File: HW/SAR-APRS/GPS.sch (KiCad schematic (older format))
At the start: 12 parts

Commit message: schematic update
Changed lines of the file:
@@
 Wire Wire Line
 	8400 2425 8400 4675
-Text GLabel 3200 2425 0    50   Input ~ 0
+Text GLabel 3200 2425 0    50   Output ~ 0
 GPS_PPS
 Text GLabel 3200 3150 0    50   Input ~ 0
 GPS_RXD
-Text GLabel 3200 3050 0    50   Input ~ 0
+Text GLabel 3200 3050 0    50   Output ~ 0
 GPS_TXD
 Wire Wire Line

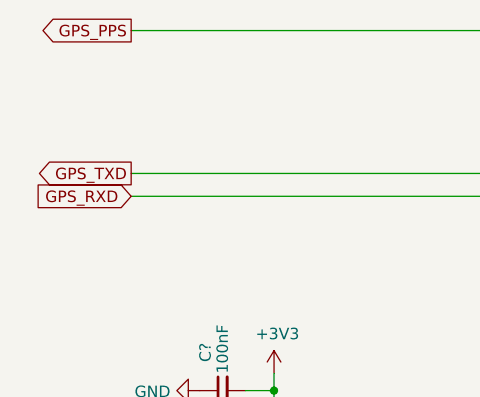
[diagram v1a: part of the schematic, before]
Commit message: schematic update
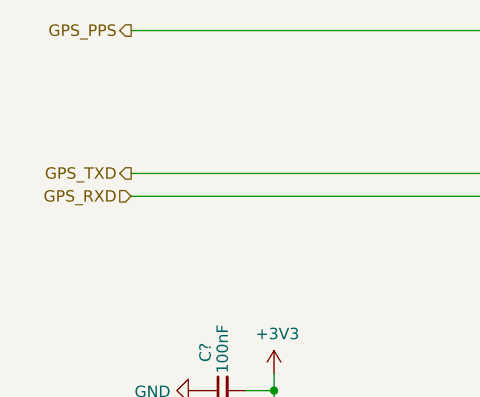
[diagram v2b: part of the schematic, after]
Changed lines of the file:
@@
 $Descr A4 11693 8268
 encoding utf-8
-Sheet 4 6
+Sheet 6 6
 Title ""
 Date ""
@@
 Wire Wire Line
 	8400 2425 8400 4675
-Text GLabel 3200 2425 0    50   Output ~ 0
+Wire Wire Line
+	4325 4375 5950 4375
+Wire Wire Line
+	4325 4475 4725 4475
+Wire Wire Line
+	4725 4475 4725 4275
+Wire Wire Line
+	4725 4275 5950 4275
+Text HLabel 3200 2425 0    50   Output ~ 0
 GPS_PPS
-Text GLabel 3200 3150 0    50   Input ~ 0
+Text HLabel 3200 3050 0    50   Output ~ 0
+GPS_TXD
+Text HLabel 3200 3150 0    50   Input ~ 0
 GPS_RXD
-Text GLabel 3200 3050 0    50   Output ~ 0
-GPS_TXD
-Wire Wire Line
-	4325 4375 5950 4375
-Wire Wire Line
-	4325 4475 4725 4475
-Wire Wire Line
-	4725 4475 4725 4275
-Wire Wire Line
-	4725 4275 5950 4275
 $EndSCHEMATC

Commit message: schem and pcb update
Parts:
- gave numbers to parts that had none: 12
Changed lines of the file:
@@
 EESchema Schematic File Version 4
 LIBS:SAR-APRS-cache
-EELAYER 28 0
+EELAYER 29 0
 EELAYER END
 $Descr A4 11693 8268
@@
 P 6025 3000
 AR Path="/5C995BB7" Ref="U?"  Part="1"
-AR Path="/5C97B601/5C995BB7" Ref="U?"  Part="1"
-F 0 "U?" H 6025 3375 50  0000 C CNN
+AR Path="/5C97B601/5C995BB7" Ref="U9"  Part="1"
+F 0 "U9" H 6025 3375 50  0000 C CNN
 F 1 "NEO_GPS_MODULE" H 6025 3284 50  0000 C CNN
 F 2 "" H 5525 3300 50  0001 C CNN
@@
 P 5525 3150
 AR Path="/5C995BBF" Ref="#PWR?"  Part="1"
-AR Path="/5C97B601/5C995BBF" Ref="#PWR?"  Part="1"
-F 0 "#PWR?" H 5525 2900 50  0001 C CNN
+AR Path="/5C97B601/5C995BBF" Ref="#PWR0148"  Part="1"
+F 0 "#PWR0148" H 5525 2900 50  0001 C CNN
 F 1 "GND" V 5530 3022 50  0000 R CNN
 F 2 "" H 5525 3150 50  0001 C CNN
@@
 P 6525 3150
 AR Path="/5C995BC5" Ref="#PWR?"  Part="1"
-AR Path="/5C97B601/5C995BC5" Ref="#PWR?"  Part="1"
-F 0 "#PWR?" H 6525 2900 50  0001 C CNN
+AR Path="/5C97B601/5C995BC5" Ref="#PWR0149"  Part="1"
+F 0 "#PWR0149" H 6525 2900 50  0001 C CNN
 F 1 "GND" V 6530 3022 50  0000 R CNN
 F 2 "" H 6525 3150 50  0001 C CNN
@@
 P 6525 2850
 AR Path="/5C995BCB" Ref="#PWR?"  Part="1"
-AR Path="/5C97B601/5C995BCB" Ref="#PWR?"  Part="1"
-F 0 "#PWR?" H 6525 2600 50  0001 C CNN
+AR Path="/5C97B601/5C995BCB" Ref="#PWR0150"  Part="1"
+F 0 "#PWR0150" H 6525 2600 50  0001 C CNN
 F 1 "GND" V 6530 2722 50  0000 R CNN
 F 2 "" H 6525 2850 50  0001 C CNN
@@
 P 5450 2750
 AR Path="/5C995BD1" Ref="#PWR?"  Part="1"
-AR Path="/5C97B601/5C995BD1" Ref="#PWR?"  Part="1"
-F 0 "#PWR?" H 5450 2600 50  0001 C CNN
+AR Path="/5C97B601/5C995BD1" Ref="#PWR0151"  Part="1"
+F 0 "#PWR0151" H 5450 2600 50  0001 C CNN
 F 1 "+3V3" H 5465 2923 50  0000 C CNN
 F 2 "" H 5450 2750 50  0001 C CNN
@@
 P 5250 2850
 AR Path="/5C995BD9" Ref="C?"  Part="1"
-AR Path="/5C97B601/5C995BD9" Ref="C?"  Part="1"
-F 0 "C?" H 5342 2896 50  0000 L CNN
+AR Path="/5C97B601/5C995BD9" Ref="C23"  Part="1"
+F 0 "C23" H 5342 2896 50  0000 L CNN
 F 1 "100nF" H 5342 2805 50  0000 L CNN
 F 2 "" H 5250 2850 50  0001 C CNN
@@
 P 5150 2850
 AR Path="/5C995BE1" Ref="#PWR?"  Part="1"
-AR Path="/5C97B601/5C995BE1" Ref="#PWR?"  Part="1"
-F 0 "#PWR?" H 5150 2600 50  0001 C CNN
+AR Path="/5C97B601/5C995BE1" Ref="#PWR0152"  Part="1"
+F 0 "#PWR0152" H 5150 2600 50  0001 C CNN
 F 1 "GND" V 5155 2722 50  0000 R CNN
 F 2 "" H 5150 2850 50  0001 C CNN
@@
 P 6700 4275
 AR Path="/5C995BE8" Ref="U?"  Part="1"
-AR Path="/5C97B601/5C995BE8" Ref="U?"  Part="1"
-F 0 "U?" H 6700 5190 50  0000 C CNN
+AR Path="/5C97B601/5C995BE8" Ref="U10"  Part="1"
+F 0 "U10" H 6700 5190 50  0000 C CNN
 F 1 "NEO-M8" H 6700 5099 50  0000 C CNN
 F 2 "" H 6250 5375 50  0001 C CNN
@@
 P 5950 3675
 AR Path="/5C995BEE" Ref="#PWR?"  Part="1"
-AR Path="/5C97B601/5C995BEE" Ref="#PWR?"  Part="1"
-F 0 "#PWR?" H 5950 3425 50  0001 C CNN
+AR Path="/5C97B601/5C995BEE" Ref="#PWR0153"  Part="1"
+F 0 "#PWR0153" H 5950 3425 50  0001 C CNN
 F 1 "GND" V 5955 3547 50  0000 R CNN
 F 2 "" H 5950 3675 50  0001 C CNN
@@
 P 5425 5025
 AR Path="/5C995BF4" Ref="#PWR?"  Part="1"
-AR Path="/5C97B601/5C995BF4" Ref="#PWR?"  Part="1"
-F 0 "#PWR?" H 5425 4775 50  0001 C CNN
+AR Path="/5C97B601/5C995BF4" Ref="#PWR0154"  Part="1"
+F 0 "#PWR0154" H 5425 4775 50  0001 C CNN
 F 1 "GND" V 5430 4897 50  0000 R CNN
 F 2 "" H 5425 5025 50  0001 C CNN
@@
 P 7450 3675
 AR Path="/5C995BFA" Ref="#PWR?"  Part="1"
-AR Path="/5C97B601/5C995BFA" Ref="#PWR?"  Part="1"
-F 0 "#PWR?" H 7450 3425 50  0001 C CNN
+AR Path="/5C97B601/5C995BFA" Ref="#PWR0155"  Part="1"
+F 0 "#PWR0155" H 7450 3425 50  0001 C CNN
 F 1 "GND" V 7455 3547 50  0000 R CNN
 F 2 "" H 7450 3675 50  0001 C CNN
@@
 P 7450 3875
 AR Path="/5C995C00" Ref="#PWR?"  Part="1"
-AR Path="/5C97B601/5C995C00" Ref="#PWR?"  Part="1"
-F 0 "#PWR?" H 7450 3625 50  0001 C CNN
+AR Path="/5C97B601/5C995C00" Ref="#PWR0156"  Part="1"
+F 0 "#PWR0156" H 7450 3625 50  0001 C CNN
 F 1 "GND" V 7455 3747 50  0000 R CNN
 F 2 "" H 7450 3875 50  0001 C CNN
@@
 P 5100 4775
 AR Path="/5C995C0D" Ref="#PWR?"  Part="1"
-AR Path="/5C97B601/5C995C0D" Ref="#PWR?"  Part="1"
-F 0 "#PWR?" H 5100 4625 50  0001 C CNN
+AR Path="/5C97B601/5C995C0D" Ref="#PWR0157"  Part="1"
+F 0 "#PWR0157" H 5100 4625 50  0001 C CNN
 F 1 "+3V3" H 5115 4948 50  0000 C CNN
 F 2 "" H 5100 4775 50  0001 C CNN
@@
 P 5600 4875
 AR Path="/5C995C16" Ref="C?"  Part="1"
-AR Path="/5C97B601/5C995C16" Ref="C?"  Part="1"
-F 0 "C?" H 5700 4900 50  0000 L CNN
+AR Path="/5C97B601/5C995C16" Ref="C26"  Part="1"
+F 0 "C26" H 5700 4900 50  0000 L CNN
 F 1 "10uF" H 5650 4800 50  0000 L CNN
 F 2 "" H 5600 4875 50  0001 C CNN
@@
 P 7850 3975
 AR Path="/5C995C1C" Ref="R?"  Part="1"
-AR Path="/5C97B601/5C995C1C" Ref="R?"  Part="1"
-F 0 "R?" H 7909 4021 50  0000 L CNN
+AR Path="/5C97B601/5C995C1C" Ref="R26"  Part="1"
+F 0 "R26" H 7909 4021 50  0000 L CNN
 F 1 "100" H 7909 3930 50  0000 L CNN
 F 2 "" H 7850 3975 50  0001 C CNN
@@
 P 8025 3875
 AR Path="/5C995C27" Ref="L?"  Part="1"
-AR Path="/5C97B601/5C995C27" Ref="L?"  Part="1"
-F 0 "L?" H 8073 3921 50  0000 L CNN
+AR Path="/5C97B601/5C995C27" Ref="L5"  Part="1"
+F 0 "L5" H 8073 3921 50  0000 L CNN
 F 1 "L_Small" H 8073 3830 50  0000 L CNN
 F 2 "" H 8025 3875 50  0001 C CNN
@@
 P 8025 3275
 AR Path="/5C995C2F" Ref="J?"  Part="1"
-AR Path="/5C97B601/5C995C2F" Ref="J?"  Part="1"
-F 0 "J?" H 8075 3525 50  0000 C CNN
+AR Path="/5C97B601/5C995C2F" Ref="J4"  Part="1"
+F 0 "J4" H 8075 3525 50  0000 C CNN
 F 1 "uFl" H 8050 3400 50  0000 C CNN
 F 2 "w_conn_rf:coaxial_u.fl-r-smt-1" H 8025 3275 50  0001 C CNN
@@
 P 7825 3275
 AR Path="/5C995C35" Ref="#PWR?"  Part="1"
-AR Path="/5C97B601/5C995C35" Ref="#PWR?"  Part="1"
-F 0 "#PWR?" H 7825 3025 50  0001 C CNN
+AR Path="/5C97B601/5C995C35" Ref="#PWR0158"  Part="1"
+F 0 "#PWR0158" H 7825 3025 50  0001 C CNN
 F 1 "GND" V 7830 3147 50  0000 R CNN
 F 2 "" H 7825 3275 50  0001 C CNN
@@
 P 5425 4875
 AR Path="/5C995C3C" Ref="C?"  Part="1"
-AR Path="/5C97B601/5C995C3C" Ref="C?"  Part="1"
-F 0 "C?" H 5550 4950 50  0000 L CNN
+AR Path="/5C97B601/5C995C3C" Ref="C25"  Part="1"
+F 0 "C25" H 5550 4950 50  0000 L CNN
 F 1 "100nF" H 5500 4875 50  0000 L CNN
 F 2 "" H 5425 4875 50  0001 C CNN
@@
 P 3825 4575
 AR Path="/5C995C4D" Ref="U?"  Part="1"
-AR Path="/5C97B601/5C995C4D" Ref="U?"  Part="1"
-F 0 "U?" H 3575 4975 60  0000 C CNN
+AR Path="/5C97B601/5C995C4D" Ref="U11"  Part="1"
+F 0 "U11" H 3575 4975 60  0000 C CNN
 F 1 "EEPROM" H 4150 4950 60  0000 C CNN
 F 2 "" H 3825 4575 60  0001 C CNN
@@
 P 3825 5075
 AR Path="/5C995C53" Ref="#PWR?"  Part="1"
-AR Path="/5C97B601/5C995C53" Ref="#PWR?"  Part="1"
-F 0 "#PWR?" H 3825 4825 50  0001 C CNN
+AR Path="/5C97B601/5C995C53" Ref="#PWR0159"  Part="1"
+F 0 "#PWR0159" H 3825 4825 50  0001 C CNN
 F 1 "GND" V 3830 4947 50  0000 R CNN
 F 2 "" H 3825 5075 50  0001 C CNN
@@
 P 3825 3925
 AR Path="/5C995C59" Ref="#PWR?"  Part="1"
-AR Path="/5C97B601/5C995C59" Ref="#PWR?"  Part="1"
-F 0 "#PWR?" H 3825 3775 50  0001 C CNN
+AR Path="/5C97B601/5C995C59" Ref="#PWR0160"  Part="1"
+F 0 "#PWR0160" H 3825 3775 50  0001 C CNN
 F 1 "+3V3" H 3840 4098 50  0000 C CNN
 F 2 "" H 3825 3925 50  0001 C CNN
@@
 P 3600 4000
 AR Path="/5C995C5F" Ref="C?"  Part="1"
-AR Path="/5C97B601/5C995C5F" Ref="C?"  Part="1"
-F 0 "C?" H 3725 4075 50  0000 L CNN
+AR Path="/5C97B601/5C995C5F" Ref="C24"  Part="1"
+F 0 "C24" H 3725 4075 50  0000 L CNN
 F 1 "100nF" H 3675 4000 50  0000 L CNN
 F 2 "" H 3600 4000 50  0001 C CNN
@@
 P 3500 4000
 AR Path="/5C995C69" Ref="#PWR?"  Part="1"
-AR Path="/5C97B601/5C995C69" Ref="#PWR?"  Part="1"
-F 0 "#PWR?" H 3500 3750 50  0001 C CNN
+AR Path="/5C97B601/5C995C69" Ref="#PWR0161"  Part="1"
+F 0 "#PWR0161" H 3500 3750 50  0001 C CNN
 F 1 "GND" V 3505 3872 50  0000 R CNN
 F 2 "" H 3500 4000 50  0001 C CNN
@@
 P 7675 5100
 AR Path="/5C995C83" Ref="D?"  Part="1"
-AR Path="/5C97B601/5C995C83" Ref="D?"  Part="1"
-F 0 "D?" V 7714 5178 50  0000 L CNN
+AR Path="/5C97B601/5C995C83" Ref="D7"  Part="1"
+F 0 "D7" V 7714 5178 50  0000 L CNN
 F 1 "LED" V 7623 5178 50  0000 L CNN
 F 2 "" H 7675 5100 50  0001 C CNN
@@
 P 7675 4850
 AR Path="/5C995C89" Ref="R?"  Part="1"
-AR Path="/5C97B601/5C995C89" Ref="R?"  Part="1"
-F 0 "R?" H 7525 4925 50  0000 L CNN
+AR Path="/5C97B601/5C995C89" Ref="R27"  Part="1"
+F 0 "R27" H 7525 4925 50  0000 L CNN
 F 1 "1k" H 7525 4825 50  0000 L CNN
 F 2 "" H 7675 4850 50  0001 C CNN
@@
 P 7450 4275
 AR Path="/5C995C8F" Ref="#PWR?"  Part="1"
-AR Path="/5C97B601/5C995C8F" Ref="#PWR?"  Part="1"
-F 0 "#PWR?" H 7450 4025 50  0001 C CNN
+AR Path="/5C97B601/5C995C8F" Ref="#PWR0162"  Part="1"
+F 0 "#PWR0162" H 7450 4025 50  0001 C CNN
 F 1 "GND" V 7455 4147 50  0000 R CNN
 F 2 "" H 7450 4275 50  0001 C CNN
@@
 P 7675 5250
 AR Path="/5C995C9B" Ref="#PWR?"  Part="1"
-AR Path="/5C97B601/5C995C9B" Ref="#PWR?"  Part="1"
-F 0 "#PWR?" H 7675 5000 50  0001 C CNN
+AR Path="/5C97B601/5C995C9B" Ref="#PWR0163"  Part="1"
+F 0 "#PWR0163" H 7675 5000 50  0001 C CNN
 F 1 "GND" V 7680 5122 50  0000 R CNN
 F 2 "" H 7675 5250 50  0001 C CNN

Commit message: schm and pcb update
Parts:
- C23, C24, C25: footprint (none) -> Capacitors_SMD:C_0603
- L5: footprint (none) -> Inductors_SMD:L_0805
- R26, R27: footprint (none) -> Resistors_SMD:R_0603
- U9: footprint (none) -> Mlab_Pin_Headers:Straight_1x04
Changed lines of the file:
@@
 F 0 "U9" H 6025 3375 50  0000 C CNN
 F 1 "NEO_GPS_MODULE" H 6025 3284 50  0000 C CNN
-F 2 "" H 5525 3300 50  0001 C CNN
+F 2 "Mlab_Pin_Headers:Straight_1x04" H 5525 3300 50  0001 C CNN
 F 3 "" H 5525 3300 50  0001 C CNN
 	1    6025 3000
@@
 F 0 "C23" H 5342 2896 50  0000 L CNN
 F 1 "100nF" H 5342 2805 50  0000 L CNN
-F 2 "" H 5250 2850 50  0001 C CNN
+F 2 "Capacitors_SMD:C_0603" H 5250 2850 50  0001 C CNN
 F 3 "~" H 5250 2850 50  0001 C CNN
 	1    5250 2850
@@
 F 0 "R26" H 7909 4021 50  0000 L CNN
 F 1 "100" H 7909 3930 50  0000 L CNN
-F 2 "" H 7850 3975 50  0001 C CNN
+F 2 "Resistors_SMD:R_0603" H 7850 3975 50  0001 C CNN
 F 3 "~" H 7850 3975 50  0001 C CNN
 	1    7850 3975
@@
 F 0 "L5" H 8073 3921 50  0000 L CNN
 F 1 "L_Small" H 8073 3830 50  0000 L CNN
-F 2 "" H 8025 3875 50  0001 C CNN
+F 2 "Inductors_SMD:L_0805" H 8025 3875 50  0001 C CNN
 F 3 "~" H 8025 3875 50  0001 C CNN
 	1    8025 3875
@@
 F 0 "C25" H 5550 4950 50  0000 L CNN
 F 1 "100nF" H 5500 4875 50  0000 L CNN
-F 2 "" H 5425 4875 50  0001 C CNN
+F 2 "Capacitors_SMD:C_0603" H 5425 4875 50  0001 C CNN
 F 3 "~" H 5425 4875 50  0001 C CNN
 	1    5425 4875
@@
 F 0 "C24" H 3725 4075 50  0000 L CNN
 F 1 "100nF" H 3675 4000 50  0000 L CNN
-F 2 "" H 3600 4000 50  0001 C CNN
+F 2 "Capacitors_SMD:C_0603" H 3600 4000 50  0001 C CNN
 F 3 "~" H 3600 4000 50  0001 C CNN
 	1    3600 4000
@@
 AR Path="/5C995C89" Ref="R?"  Part="1"
 AR Path="/5C97B601/5C995C89" Ref="R27"  Part="1"
-F 0 "R27" H 7525 4925 50  0000 L CNN
+F 0 "R27" H 7475 4900 50  0000 L CNN
 F 1 "1k" H 7525 4825 50  0000 L CNN
-F 2 "" H 7675 4850 50  0001 C CNN
+F 2 "Resistors_SMD:R_0603" H 7675 4850 50  0001 C CNN
 F 3 "~" H 7675 4850 50  0001 C CNN
 	1    7675 4850

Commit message: PCB update
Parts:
- C23, C24, C25: footprint Capacitors_SMD:C_0603 -> Capacitors_SMD:C_0805
- C26: footprint (none) -> Capacitors_SMD:C_1210
- D7: footprint (none) -> LEDs:LED_0805
- R26, R27: footprint Resistors_SMD:R_0603 -> Resistors_SMD:R_0805
- U10: footprint (none) -> RF_GPS:ublox_NEO
- U11: footprint (none) -> IO:TSSOP-8_4.4x3mm_P0.65mm
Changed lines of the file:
@@
 F 0 "C23" H 5342 2896 50  0000 L CNN
 F 1 "100nF" H 5342 2805 50  0000 L CNN
-F 2 "Capacitors_SMD:C_0603" H 5250 2850 50  0001 C CNN
+F 2 "Capacitors_SMD:C_0805" H 5250 2850 50  0001 C CNN
 F 3 "~" H 5250 2850 50  0001 C CNN
 	1    5250 2850
@@
 F 0 "U10" H 6700 5190 50  0000 C CNN
 F 1 "NEO-M8" H 6700 5099 50  0000 C CNN
-F 2 "" H 6250 5375 50  0001 C CNN
+F 2 "RF_GPS:ublox_NEO" H 6250 5375 50  0001 C CNN
 F 3 "" H 6250 5375 50  0001 C CNN
 	1    6700 4275
@@
 F 0 "C26" H 5700 4900 50  0000 L CNN
 F 1 "10uF" H 5650 4800 50  0000 L CNN
-F 2 "" H 5600 4875 50  0001 C CNN
+F 2 "Capacitors_SMD:C_1210" H 5600 4875 50  0001 C CNN
 F 3 "~" H 5600 4875 50  0001 C CNN
 	1    5600 4875
@@
 F 0 "R26" H 7909 4021 50  0000 L CNN
 F 1 "100" H 7909 3930 50  0000 L CNN
-F 2 "Resistors_SMD:R_0603" H 7850 3975 50  0001 C CNN
+F 2 "Resistors_SMD:R_0805" H 7850 3975 50  0001 C CNN
 F 3 "~" H 7850 3975 50  0001 C CNN
 	1    7850 3975
@@
 F 0 "C25" H 5550 4950 50  0000 L CNN
 F 1 "100nF" H 5500 4875 50  0000 L CNN
-F 2 "Capacitors_SMD:C_0603" H 5425 4875 50  0001 C CNN
+F 2 "Capacitors_SMD:C_0805" H 5425 4875 50  0001 C CNN
 F 3 "~" H 5425 4875 50  0001 C CNN
 	1    5425 4875
@@
 F 0 "U11" H 3575 4975 60  0000 C CNN
 F 1 "EEPROM" H 4150 4950 60  0000 C CNN
-F 2 "" H 3825 4575 60  0001 C CNN
+F 2 "IO:TSSOP-8_4.4x3mm_P0.65mm" H 3825 4575 60  0001 C CNN
 F 3 "" H 3825 4575 60  0001 C CNN
 	1    3825 4575
@@
 F 0 "C24" H 3725 4075 50  0000 L CNN
 F 1 "100nF" H 3675 4000 50  0000 L CNN
-F 2 "Capacitors_SMD:C_0603" H 3600 4000 50  0001 C CNN
+F 2 "Capacitors_SMD:C_0805" H 3600 4000 50  0001 C CNN
 F 3 "~" H 3600 4000 50  0001 C CNN
 	1    3600 4000
@@
 F 0 "D7" V 7714 5178 50  0000 L CNN
 F 1 "LED" V 7623 5178 50  0000 L CNN
-F 2 "" H 7675 5100 50  0001 C CNN
+F 2 "LEDs:LED_0805" H 7675 5100 50  0001 C CNN
 F 3 "~" H 7675 5100 50  0001 C CNN
 	1    7675 5100
@@
 F 0 "R27" H 7475 4900 50  0000 L CNN
 F 1 "1k" H 7525 4825 50  0000 L CNN
-F 2 "Resistors_SMD:R_0603" H 7675 4850 50  0001 C CNN
+F 2 "Resistors_SMD:R_0805" H 7675 4850 50  0001 C CNN
 F 3 "~" H 7675 4850 50  0001 C CNN
 	1    7675 4850
